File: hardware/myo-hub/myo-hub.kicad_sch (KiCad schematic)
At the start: 44 parts, among them IC1 AD4130-8BCPZ-RL7, J1 Conn_01x03, J10 Conn_01x03, J11 Conn_01x03, J12 Conn_01x03, J13 Conn_01x03, J14 Conn_01x03, J15 Conn_01x03, J16 Conn_01x03, J2 Conn_01x03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

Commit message: Change ADC to AD7124-8
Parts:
- removed IC1: AD4130-8BCPZ-RL7, myo-hub:QFN50P500X500X80-33N-D, symbol AD4130:AD4130-8BCPZ-RL7
- removed J16: Conn_01x03, Connector_JST:JST_PH_B3B-PH-K_1x03_P2.00mm_Vertical, symbol Connector_Generic:Conn_01x03
- removed R22: 1M, Resistor_SMD:R_0603_1608Metric_Pad0.98x0.95mm_HandSolder, symbol Device:R
- added IC1: AD7124-8BBCPZ-RL7, myo-hub:QFN50P500X500X100-33N-D, symbol AD7124-8:AD7124-8BBCPZ-RL7
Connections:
- net GND: now also IC1.12 (REFIN1(+)), IC1.13 (REFIN1(-)), IC1.21 (AIN15/IOUT/VBIAS/REFIN2(-)), IC1.22 (REFOUT), IC1.23 (AVSS), IC1.25 (PSW), IC1.3 (DGND), IC1.31 (CLK), IC1.33 (EP)
- net MISO: now also IC1.28 (DOUT/~{RDY})
- net MOSI: now also IC1.29 (DIN)
- net SCK: now also IC1.30 (SCLK)
- net V0: now also IC1.20 (AIN14/IOUT/VBIAS/REFIN2(+))
- net V1: now also IC1.18 (AIN12/IOUT/VBIAS)
- net V10: now also IC1.8 (AIN4/IOUT/VBIAS/P3)
- net V11: now also IC1.10 (AIN6/IOUT/VBIAS)
- net V12: now also IC1.15 (AIN9/IOUT/VBIAS)
- net V13: now also IC1.17 (AIN11/IOUT/VBIAS)
- net V14: now also IC1.19 (AIN13/IOUT/VBIAS)
- net V2: now also IC1.16 (AIN10/IOUT/VBIAS)
- net V3: now also IC1.14 (AIN8/IOUT/VBIAS)
- net V4: now also IC1.11 (AIN7/IOUT/VBIAS)
- net V5: now also IC1.9 (AIN5/IOUT/VBIAS/P4)
- net V6: now also IC1.7 (AIN3/IOUT/VBIAS/P2)
- net V7: now also IC1.5 (AIN1/IOUT/VBIAS)
- net V8: now also IC1.4 (AIN0/IOUT/VBIAS)
- net V9: now also IC1.6 (AIN2/IOUT/VBIAS/P1)
- net VCC: now also IC1.2 (IOVDD), IC1.27 (~{SYNC})
- net VDDA: now also IC1.26 (AVDD)
- net ~{SS}: now also IC1.32 (~{CS})
- net at C5.1: now also IC1.24 (REGCAPA)
- net at C4.2: now also IC1.1 (REGCAPD)
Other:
- moved on the sheet: C5

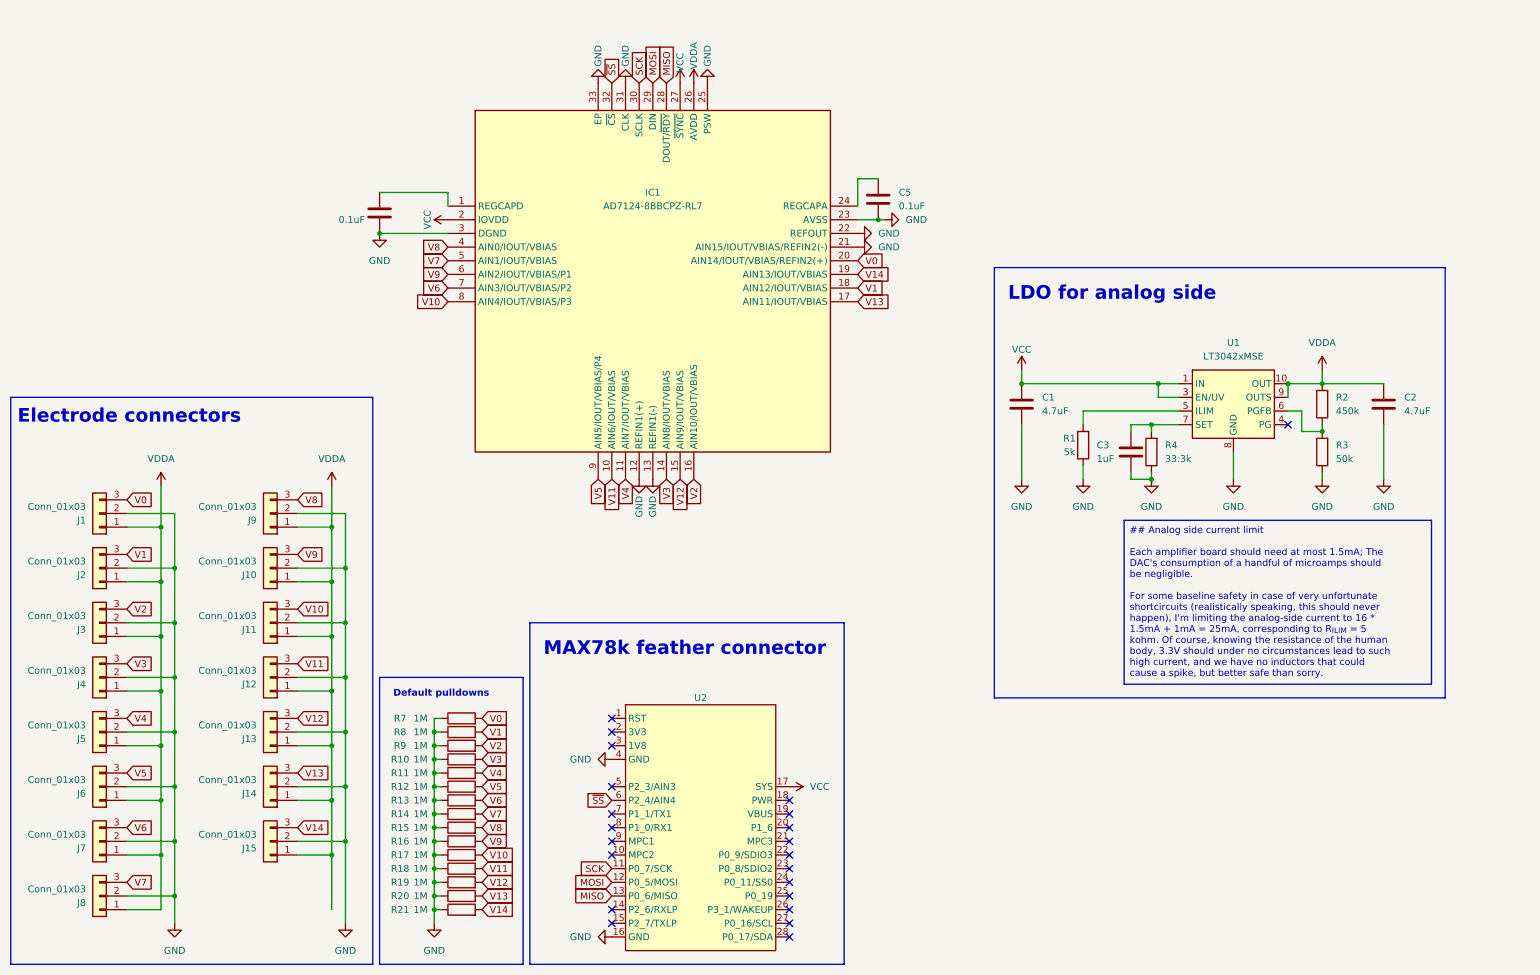
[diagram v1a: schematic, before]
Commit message: Tidy mainboard schematic
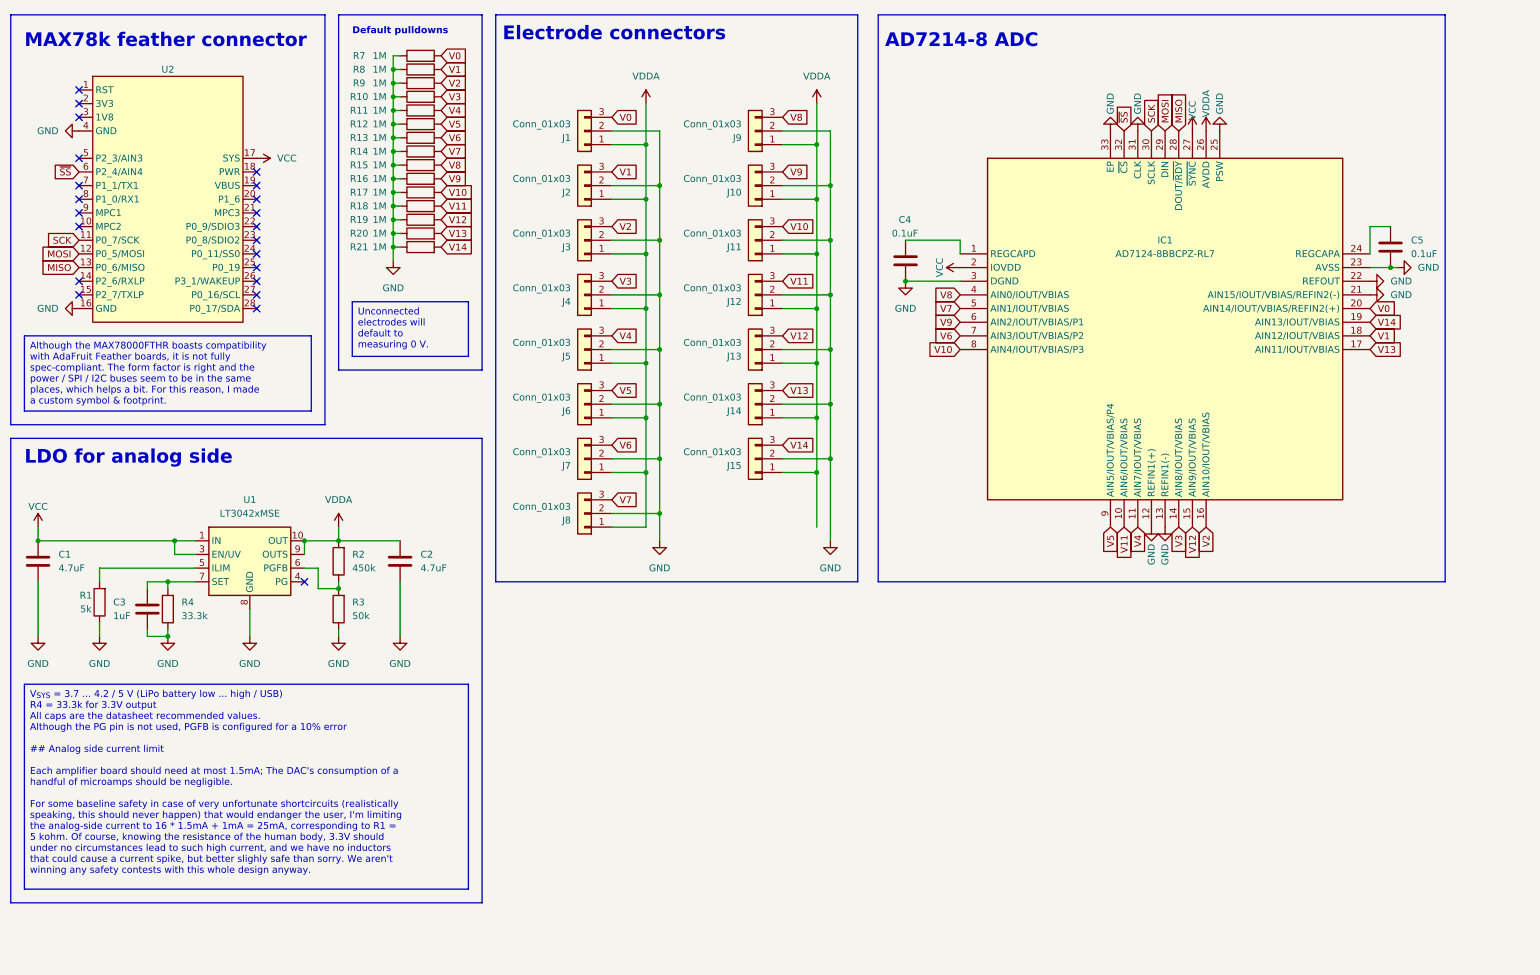
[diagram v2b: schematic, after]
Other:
- note added: "AD7214-8 ADC"
- moved on the sheet: C1, C2, C3, C5, IC1, J1, J10, J11, J12, J13, J14, J15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

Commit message: Mainboard layout cleanup
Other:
- title: (none) -> 15 Channel EMG feather wing
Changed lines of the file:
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@@
 (kicad_sch (version 20230121) (generator eeschema)
   (paper "A4")
+  (title_block
+    (title "15 Channel EMG feather wing")
+  )
   (junction (at 167.64 87.63) (diameter 0) (color 0 0 0 0)
   )
@@
   )
   (junction (at 271.78 62.23) (diameter 0) (color 0 0 0 0)
-  )
-  (junction (at 165.1 100.33) (diameter 0) (color 0 0 0 0)
   )
   (junction (at 167.64 97.79) (diameter 0) (color 0 0 0 0)
@@
     (stroke (width 0) (type default))
   )
-  (wire (pts (xy 165.1 110.49) (xy 165.1 100.33))
-    (stroke (width 0) (type default))
-  )
   (wire (pts (xy 158.75 67.31) (xy 167.64 67.31))
     (stroke (width 0) (type default))
@@
     (stroke (width 0) (type default))
   )
-  (rectangle (start 176.53 15.24) (end 281.94 120.65)
+  (rectangle (start 176.53 15.24) (end 281.94 139.7)
     (stroke (width 0) (type default))
     (fill (type none))
@@
     (fill (type none))
   )
-  (text_box "Although the MAX78000FTHR boasts compatibility with AdaFruit Feather boards, it is not fully spec-compliant. The form factor is right and the power / SPI / I2C buses seem to be in the same places, which helps a bit. For this reason, I made a custom symbol & footprint."
+  (text_box "Voltages on the skin are around 10 - 1000 uV (if electrodes placed properly), and may, in extreme cases, rise to 10 mV, give or take (not considering ESD). The active electrode boards have a gain of 160, bringing the nominal interval to 1.6 - 160 mV around the AVDD/2 bias (extreme case, VDD/2 +- 1.6 V). The internal PGAs may be used to add up to another 128x gain, if AIN15 is properly set to AVDD/2 (so the PGAs don't saturate). Otherwise, I'm using a very basic configuration for the ADC pins. The electrode order is chosen to facilitate routing."
+    (at 179.07 121.92 0) (size 100.33 15.24)
+    (stroke (width 0) (type default))
+    (fill (type none))
+    (effects (font (size 1.27 1.27)) (justify left top))
+  )
+  (text_box "Although the MAX78000FTHR boasts compatibility with AdaFruit Feather boards, it is not fully spec-compliant. The form factor is right and the power / SPI / I2C buses seem to be in the same places, which helps a bit. Yet I still made a custom symbol & footprint."
     (at 17.78 74.93 0) (size 53.34 13.97)
     (stroke (width 0) (type default))
@@
     (effects (font (size 1.27 1.27)) (justify left top))
   )
-  (text_box "V_{SYS} = 3.7 ... 4.2 / 5 V (LiPo battery low ... high / USB)\nR4 = 33.3k for 3.3V output\nAll caps are the datasheet recommended values.\nAlthough the PG pin is not used, PGFB is configured for a 10% error\n\n## Analog side current limit\n\nEach amplifier board should need at most 1.5mA; The DAC's consumption of a handful of microamps should be negligible.\n\nFor some baseline safety in case of very unfortunate shortcircuits (realistically speaking, this should never happen) that would endanger the user, I'm limiting the analog-side current to 16 * 1.5mA + 1mA = 25mA, corresponding to R1 = 5 kohm. Of course, knowing the resistance of the human body, 3.3V should under no circumstances lead to such high current, and we have no inductors that could cause a current spike, but better slighly safe than sorry. We aren't winning any safety contests with this whole design anyway.\n"
+  (text_box "V_{SYS} = 3.7 ... 4.2 / 5 V (LiPo battery low ... high / USB)\nR4 = 33.3k for 3.3V output\nAll caps are the datasheet recommended values.\nAlthough the PG pin is not used, PGFB is configured for a 10% error\n\n## Analog side current limit\n\nEach amplifier board should need at most 1.5mA; The DAC's consumption of a handful of microamps should be negligible.\n\nFor some baseline safety in case of very unfortunate shortcircuits that would endanger the user (which, realistically speaking, should never happen), I'm limiting the analog-side current to 16 * 1.5mA + 1mA = 25mA, corresponding to R1 = 5 kohm. Of course, knowing the resistance of the human body, 3.3V should under no circumstances lead to such high current, and we have no inductors that could cause a current spike, but better slighly safe than sorry. We aren't winning any safety contests with this whole design anyway.\n"
     (at 17.78 139.7 0) (size 82.55 38.1)
     (stroke (width 0) (type default))

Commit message: Add pseudo-differential reference circuit
This in turn enables us to use the PGAs without saturating them.

With a zero reference, we can only use gain=1, because even gain=2
would result in a AVDD/2*2 = AVDD voltage at the PGA's output with
zero! input.
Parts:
- added C6: 0.1uF, Capacitor_SMD:C_0603_1608Metric_Pad1.08x0.95mm_HandSolder, symbol Device:C
- added R5, R6: 500k 1%, Resistor_SMD:R_0603_1608Metric_Pad0.98x0.95mm_HandSolder, symbol Device:R
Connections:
- net GND: now also C6.2, R6.1; no longer IC1.21 (AIN15/IOUT/VBIAS/REFIN2(-))
- net VDDA: now also R5.2
- new net COM: C6.1, IC1.21 (AIN15/IOUT/VBIAS/REFIN2(-)), R5.1, R6.2
